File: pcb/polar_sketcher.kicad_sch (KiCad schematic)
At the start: 31 parts, among them J1 LIMIT_1, J10 SERVO_PINS, J11 ENCODER, J12 ESP_H_1, J13 RPi_H_1, J14 RPi_H_2, J2 LIMIT_3, J3 STEPPER_1, J4 ESP_H_1, J5 ESP_H_2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

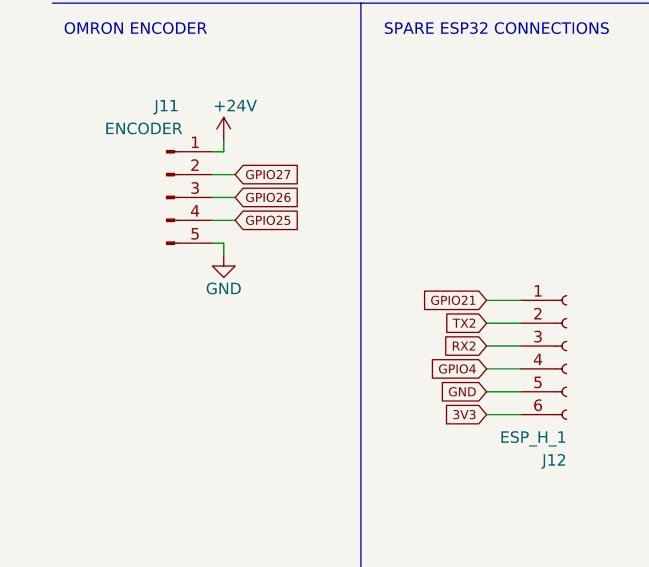
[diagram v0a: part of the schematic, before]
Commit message: fix design flaw in PCB that makes it fry the esp32 if you connect the encoder the opposite way around
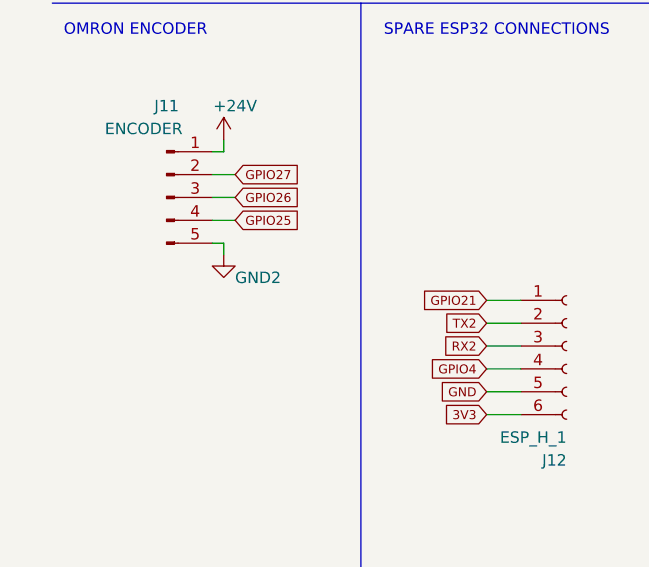
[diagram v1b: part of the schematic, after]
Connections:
- net GND: no longer J11.5 (Pin_5)
- net GND2: now also J11.5 (Pin_5)
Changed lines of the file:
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@@
     (pin "2")
+  )
+  (symbol (lib_id "power:GND2") (at 31.75 153.67 0) (unit 1)
+    (in_bom yes) (on_board yes)
+    (property "Reference" "#PWR?" (id 0) (at 31.75 160.02 0)
+      (effects (font (size 1.27 1.27)) hide)
+    )
+    (property "Value" "GND2" (id 1) (at 35.56 156.2418 0))
+    (property "Footprint" "" (id 2) (at 31.75 153.67 0)
+      (effects (font (size 1.27 1.27)) hide)
+    )
+    (property "Datasheet" "" (id 3) (at 31.75 153.67 0)
+      (effects (font (size 1.27 1.27)) hide)
+    )
+    (pin "1")
   )
   (symbol (lib_id "Connector:Conn_01x02_Male") (at 118.11 35.56 0) (unit 1)
@@
     (pin "1")
   )
-  (symbol (lib_id "power:GND") (at 31.75 153.67 0) (unit 1)
-    (in_bom yes) (on_board yes)
-    (property "Reference" "#PWR024" (id 0) (at 31.75 160.02 0)
-      (effects (font (size 1.27 1.27)) hide)
-    )
-    (property "Value" "GND" (id 1) (at 31.75 157.48 0))
-    (property "Footprint" "" (id 2) (at 31.75 153.67 0)
-      (effects (font (size 1.27 1.27)) hide)
-    )
-    (property "Datasheet" "" (id 3) (at 31.75 153.67 0)
-      (effects (font (size 1.27 1.27)) hide)
-    )
-    (pin "1")
-  )
   (symbol (lib_id "Driver_Motor:Pololu_Breakout_A4988") (at 76.2 90.17 0) (unit 1)
     (in_bom yes) (on_board yes)
@@
       (reference "#PWR023") (unit 1) (value "GND") (footprint "")
     )
-    (path "/597d889a-c427-4051-9abc-5179944660da"
-      (reference "#PWR024") (unit 1) (value "GND") (footprint "")
-    )
     (path "/09b34bd2-3bb1-4d66-8249-92246024bf21"
       (reference "#PWR0101") (unit 1) (value "GND2") (footprint "")
@@
       (reference "#PWR0106") (unit 1) (value "+3V3") (footprint "")
     )
+    (path "/1d7648a9-9e5d-4388-a200-b0b1a89c47c6"
+      (reference "#PWR?") (unit 1) (value "GND2") (footprint "")
+    )
     (path "/3f012fe6-0af3-4448-8f34-de5fc294a4ac"
